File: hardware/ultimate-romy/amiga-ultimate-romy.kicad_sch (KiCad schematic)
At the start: 7 parts, among them IC2 FAT_GARY, U1 ATF22V10C-XU, U2 ATF22V10C-XU

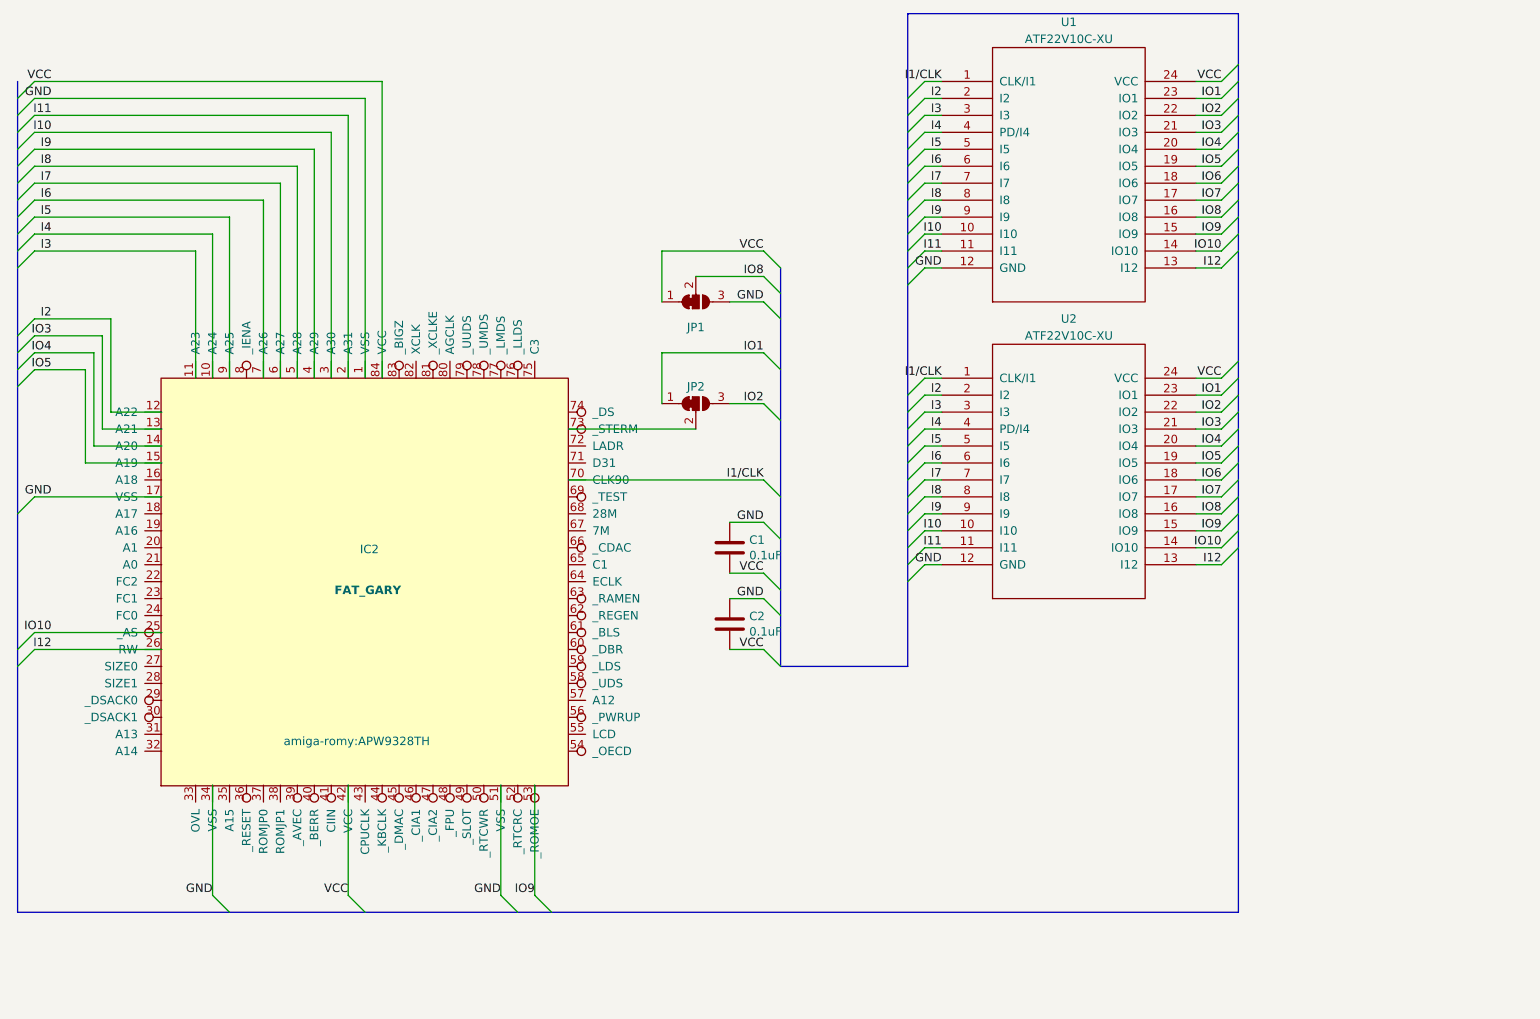
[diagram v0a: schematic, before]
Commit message: Update Ultimate ROMY to Rev6
- Reroute the board to use 6mil instead of 5mil traces.
  This will make the boards significantly cheaper with some fab houses
- Add address pins for 4MB support
- Move vias in PLCC footprint to the outside to prevent solder paste
  from leaking to the other side when using hot air to assemble socket
  on A4000 version
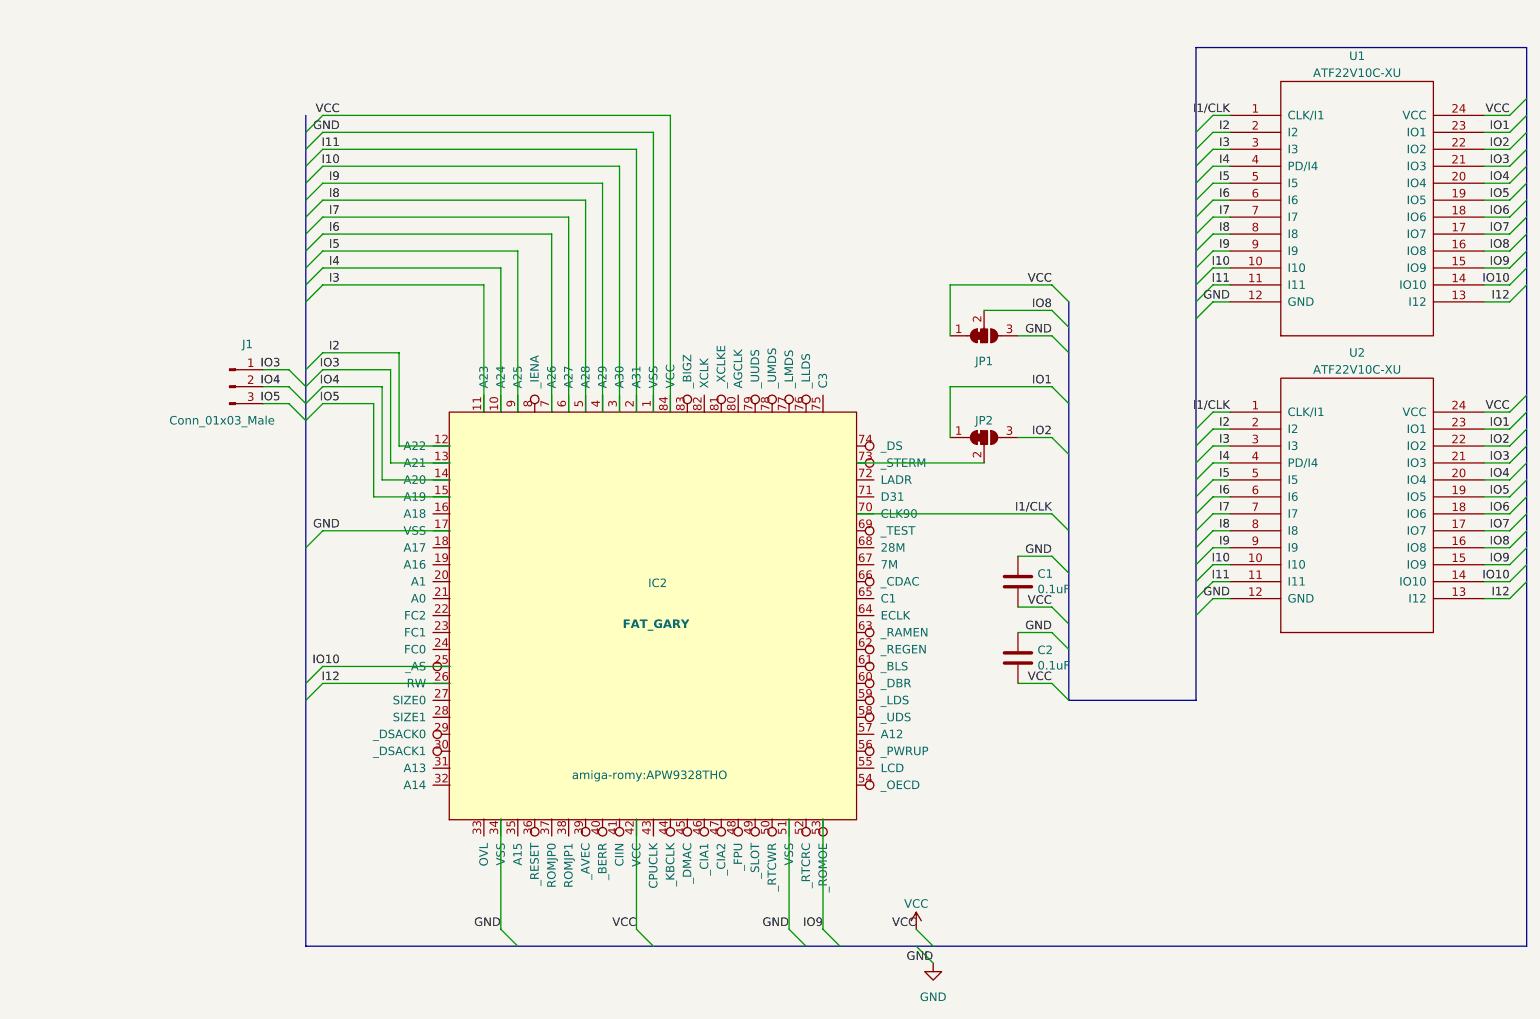
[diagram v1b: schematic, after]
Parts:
- added J1: Conn_01x03_Male, Connector_PinHeader_2.54mm:PinHeader_1x03_P2.54mm_Vertical, symbol Connector:Conn_01x03_Male
- IC2: footprint amiga-romy:APW9328TH -> amiga-romy:APW9328THO
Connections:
- net IO3: now also J1.1 (Pin_1)
- net IO4: now also J1.2 (Pin_2)
- net IO5: now also J1.3 (Pin_3)
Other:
- moved on the sheet: C1, C2, IC2, JP1, JP2, U1, U2
